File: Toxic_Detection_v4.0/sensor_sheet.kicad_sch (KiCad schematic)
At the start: 22 parts, among them IC4 ADS7828E_2K5, IC5 ADS7828E_2K5, IC6 ADS7828E_2K5, J6 79107-7205, J7 79107-7205, J8 Conn_01x06_Pin, Q1 BSS138-G, Q2 BSS138-G

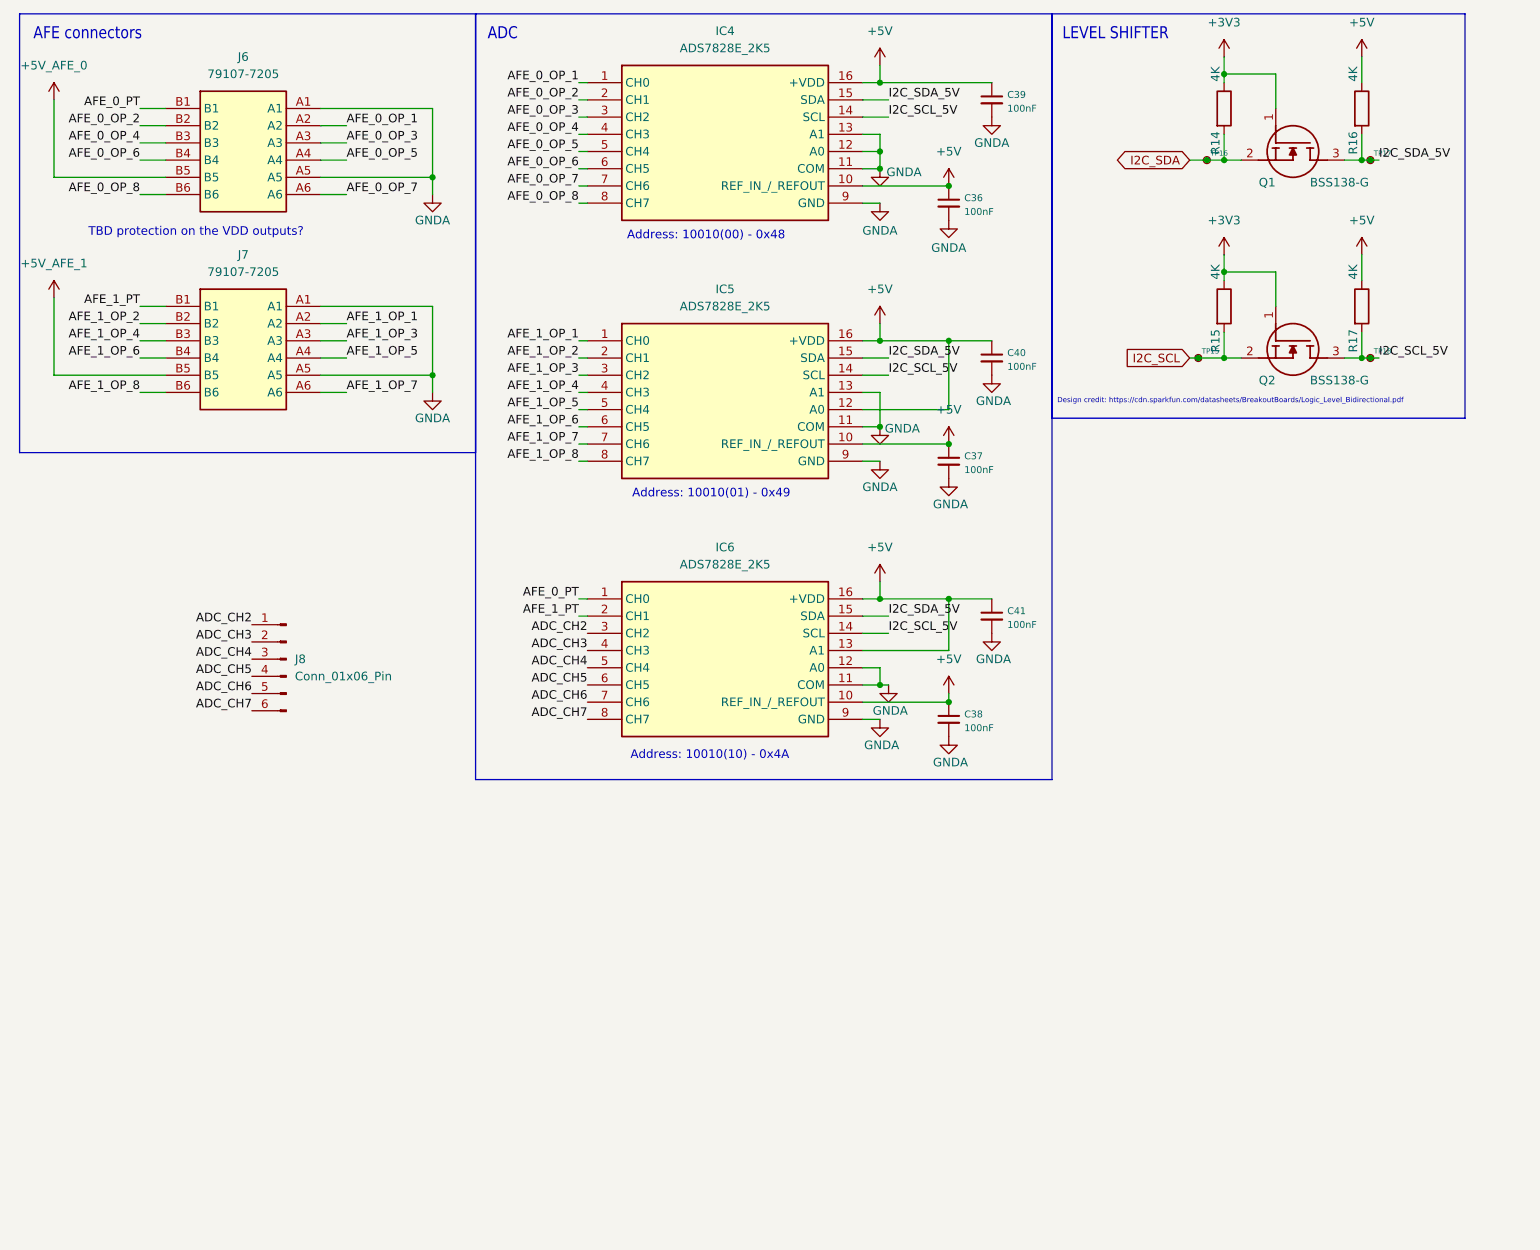
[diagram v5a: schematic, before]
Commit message: feat: take into account all reviews: add anti-aliasing filters, upgrade 3V3 LDO to support up to 5A, fix UART bug between STM and GNSS
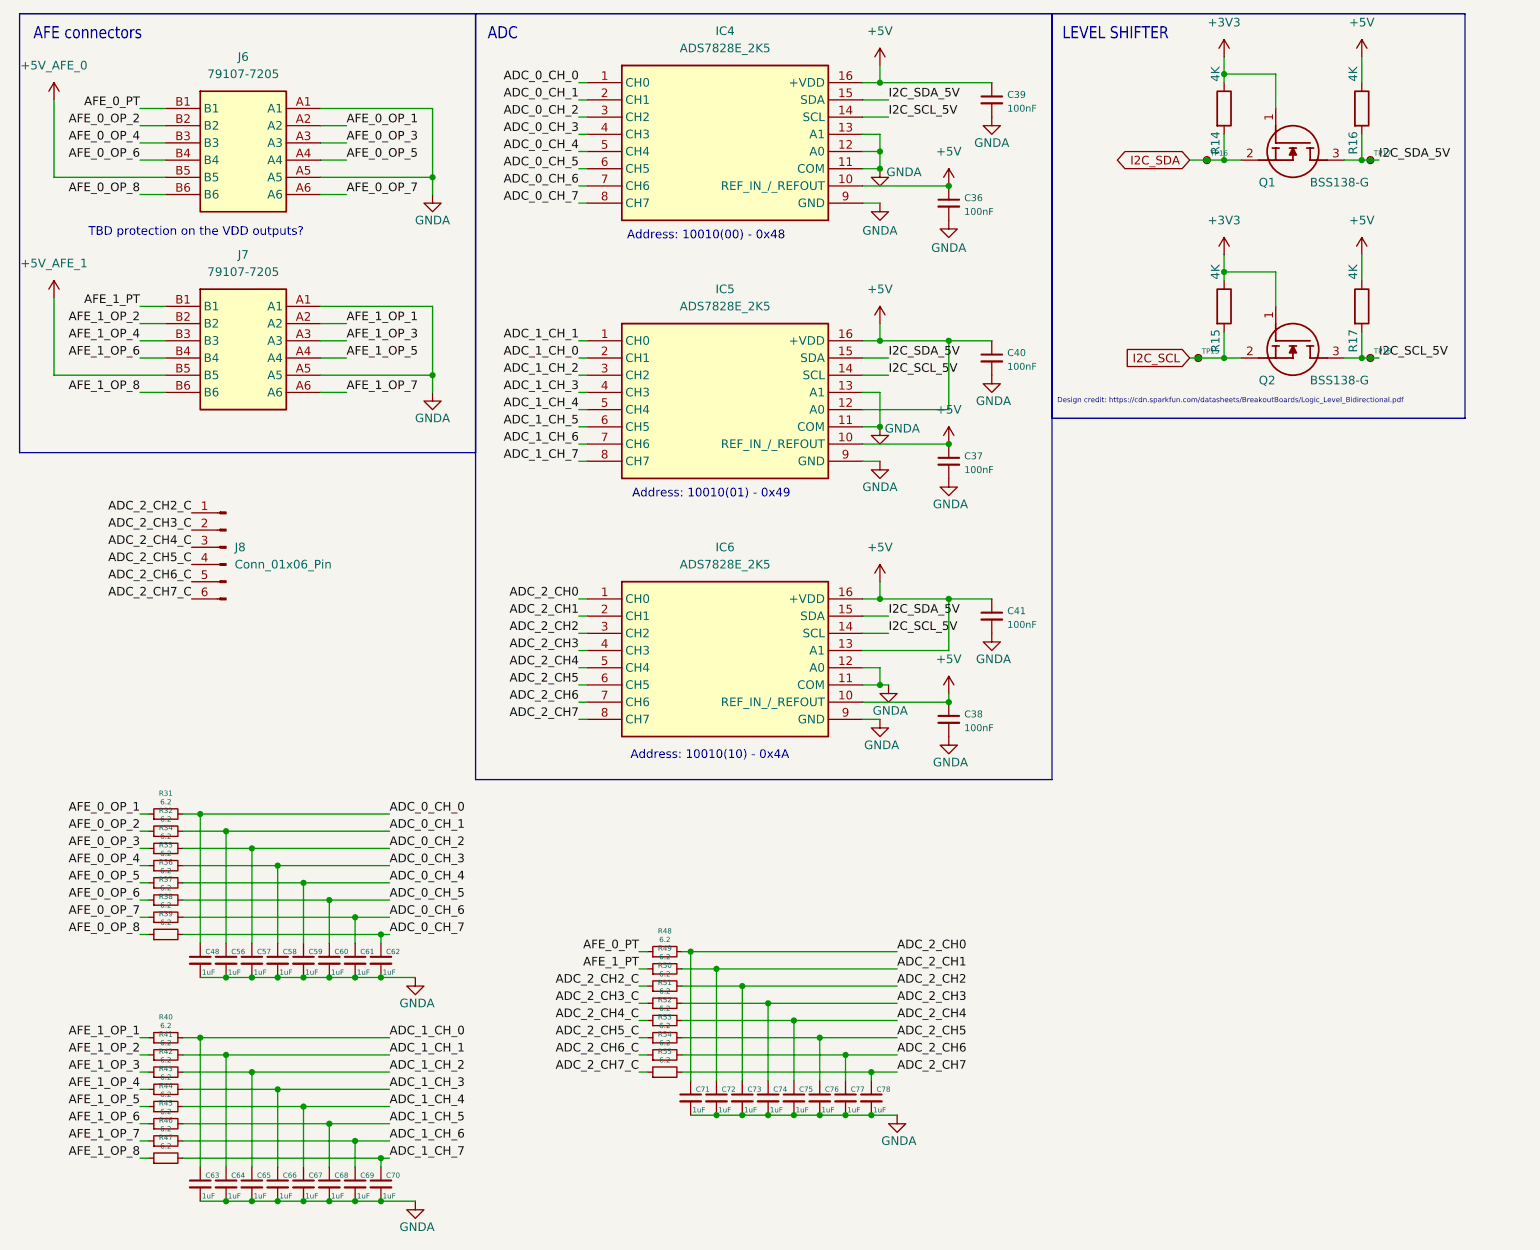
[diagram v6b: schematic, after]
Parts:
- added C48, C56, C57, C58, C59, C60, C61, C62, C63, C64, C65, C66, C67, C68, C69, C70, C71, C72, C73, C74, C75, C76, C77, C78: 1uF, Capacitor_SMD:C_0805_2012Metric_Pad1.18x1.45mm_HandSolder, symbol Device:C_Small
- added R31, R32, R34, R35, R36, R37, R38, R39, R40, R41, R42, R43, R44, R45, R46, R47, R48, R49, R50, R51, R52, R53, R54, R55: 6.2, Resistor_SMD:R_0805_2012Metric_Pad1.20x1.40mm_HandSolder, symbol Device:R_Small
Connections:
- net AFE_0_OP_1: now also R31.1; no longer IC4.1 (CH0)
- net AFE_0_OP_2: now also R32.1; no longer IC4.2 (CH1)
- net AFE_0_OP_3: now also R34.1; no longer IC4.3 (CH2)
- net AFE_0_OP_4: now also R35.1; no longer IC4.4 (CH3)
- net AFE_0_OP_5: now also R36.1; no longer IC4.5 (CH4)
- net AFE_0_OP_6: now also R37.1; no longer IC4.6 (CH5)
- net AFE_0_OP_7: now also R38.1; no longer IC4.7 (CH6)
- net AFE_0_OP_8: now also R39.1; no longer IC4.8 (CH7)
- net AFE_0_PT: now also R48.1; no longer IC6.1 (CH0)
- net AFE_1_OP_1: now also R40.1; no longer IC5.1 (CH0)
- net AFE_1_OP_2: now also R41.1; no longer IC5.2 (CH1)
- net AFE_1_OP_3: now also R42.1; no longer IC5.3 (CH2)
- net AFE_1_OP_4: now also R43.1; no longer IC5.4 (CH3)
- net AFE_1_OP_5: now also R44.1; no longer IC5.5 (CH4)
- net AFE_1_OP_6: now also R45.1; no longer IC5.6 (CH5)
- net AFE_1_OP_7: now also R46.1; no longer IC5.7 (CH6)
- net AFE_1_OP_8: now also R47.1; no longer IC5.8 (CH7)
- net AFE_1_PT: now also R49.1; no longer IC6.2 (CH1)
- net GNDA: now also C48.2, C56.2, C57.2, C58.2, C59.2, C60.2, C61.2, C62.2, C63.2, C64.2, C65.2, C66.2, C67.2, C68.2, C69.2, C70.2, C71.2, C72.2, C73.2, C74.2, C75.2, C76.2, C77.2, C78.2
- net ADC_CH2 renamed ADC_2_CH2
- net ADC_2_CH2: now also C73.1, R50.2; no longer J8.1 (Pin_1)
- net ADC_CH3 renamed ADC_2_CH3
- net ADC_2_CH3: now also C74.1, R51.2; no longer J8.2 (Pin_2)
- net ADC_CH4 renamed ADC_2_CH4
- net ADC_2_CH4: now also C75.1, R52.2; no longer J8.3 (Pin_3)
- net ADC_CH5 renamed ADC_2_CH5
- net ADC_2_CH5: now also C76.1, R53.2; no longer J8.4 (Pin_4)
- net ADC_CH6 renamed ADC_2_CH6
- net ADC_2_CH6: now also C77.1, R54.2; no longer J8.5 (Pin_5)
- net ADC_CH7 renamed ADC_2_CH7
- net ADC_2_CH7: now also C78.1, R55.2; no longer J8.6 (Pin_6)
- new net ADC_0_CH_0: C48.1, IC4.1 (CH0), R31.2
- new net ADC_0_CH_1: C56.1, IC4.2 (CH1), R32.2
- new net ADC_0_CH_2: C57.1, IC4.3 (CH2), R34.2
- new net ADC_0_CH_3: C58.1, IC4.4 (CH3), R35.2
- new net ADC_0_CH_4: C59.1, IC4.5 (CH4), R36.2
- new net ADC_0_CH_5: C60.1, IC4.6 (CH5), R37.2
- new net ADC_0_CH_6: C61.1, IC4.7 (CH6), R38.2
- new net ADC_0_CH_7: C62.1, IC4.8 (CH7), R39.2
- new net ADC_1_CH_0: C63.1, IC5.2 (CH1), R40.2
- new net ADC_1_CH_1: C64.1, IC5.1 (CH0), R41.2
- new net ADC_1_CH_2: C65.1, IC5.3 (CH2), R42.2
- new net ADC_1_CH_3: C66.1, IC5.4 (CH3), R43.2
- new net ADC_1_CH_4: C67.1, IC5.5 (CH4), R44.2
- new net ADC_1_CH_5: C68.1, IC5.6 (CH5), R45.2
- new net ADC_1_CH_6: C69.1, IC5.7 (CH6), R46.2
- new net ADC_1_CH_7: C70.1, IC5.8 (CH7), R47.2
- new net ADC_2_CH0: C71.1, IC6.1 (CH0), R48.2
- new net ADC_2_CH1: C72.1, IC6.2 (CH1), R49.2
- new net ADC_2_CH2_C: J8.1 (Pin_1), R50.1
- new net ADC_2_CH3_C: J8.2 (Pin_2), R51.1
- new net ADC_2_CH4_C: J8.3 (Pin_3), R52.1
- new net ADC_2_CH5_C: J8.4 (Pin_4), R53.1
- new net ADC_2_CH6_C: J8.5 (Pin_5), R54.1
- new net ADC_2_CH7_C: J8.6 (Pin_6), R55.1
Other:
- moved on the sheet: J8

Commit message: feat: generate gerber, bom, and prepare mouser order
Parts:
- R14, R15, R16, R17: value 4K -> 10k
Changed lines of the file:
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@@
 			)
 		)
-		(property "Value" "4K"
+		(property "Value" "10k"
 			(at 189.23 21.59 90)
 			(effects
@@
 			)
 		)
-		(property "Value" "4K"
+		(property "Value" "10k"
 			(at 189.23 50.8 90)
 			(effects
@@
 			)
 		)
-		(property "Value" "4K"
+		(property "Value" "10k"
 			(at 209.55 50.8 90)
 			(effects
@@
 			)
 		)
-		(property "Value" "4K"
+		(property "Value" "10k"
 			(at 209.55 21.59 90)
 			(effects
